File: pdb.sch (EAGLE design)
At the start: 43 parts, among them J1 XT60PWFEMALE, Q1 IRFR5305PBF, Q2 IRFR5305PBF, Q3 20MHz, U1 TSR_1-2433, U2 TXB0104, U3 ATMEGA48-20AU, U4 LTC2946CMSPBF, U5 LTC2946CMSPBF, U6 LTC2946CMSPBF, U7 AT30TS74SS8M

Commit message: fixed 3d models
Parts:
- C1, C2, C3, C4, C5, C6, C7: device resistor:C-EUC0603 -> rcl:C-EUC0603
- R1, R10, R11, R2, R6, R7, R8, R9: device resistor:R-EU_R0603 -> rcl:R-EU_R0603
- U4: SPICEPREFIX (none) -> X
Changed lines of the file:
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@@
 <part name="Q1" library="transistor-power" library_urn="urn:adsk.eagle:library:400" deviceset="IRF?5305" device="R" package3d_urn="urn:adsk.eagle:package:29503/2" value="IRFR5305PBF"/>
 <part name="D1" library="diode" library_urn="urn:adsk.eagle:library:210" deviceset="DIODE-" device="DO214BA" package3d_urn="urn:adsk.eagle:package:43453/2" value="ZD18"/>
-<part name="R2" library="resistor" library_urn="urn:adsk.eagle:library:348" deviceset="R-EU_" device="R0603" package3d_urn="urn:adsk.eagle:package:26057/1" value="10k"/>
+<part name="R2" library="rcl" library_urn="urn:adsk.eagle:library:334" deviceset="R-EU_" device="R0603" package3d_urn="urn:adsk.eagle:package:23555/2" value="10k"/>
 <part name="Q2" library="transistor-power" library_urn="urn:adsk.eagle:library:400" deviceset="IRF?5305" device="R" package3d_urn="urn:adsk.eagle:package:29503/2" value="IRFR5305PBF"/>
-<part name="R1" library="resistor" library_urn="urn:adsk.eagle:library:348" deviceset="R-EU_" device="R0603" package3d_urn="urn:adsk.eagle:package:26057/1" value="1k"/>
+<part name="R1" library="rcl" library_urn="urn:adsk.eagle:library:334" deviceset="R-EU_" device="R0603" package3d_urn="urn:adsk.eagle:package:23555/2" value="1k"/>
 <part name="GND2" library="supply1" deviceset="GND" device=""/>
 <part name="SUPPLY2" library="supply2" library_urn="urn:adsk.eagle:library:372" deviceset="V+" device=""/>
@@
 <part name="SUPPLY7" library="supply2" library_urn="urn:adsk.eagle:library:372" deviceset="+5V" device=""/>
 <part name="+3V32" library="supply1" library_urn="urn:adsk.eagle:library:371" deviceset="+3V3" device=""/>
-<part name="R6" library="resistor" library_urn="urn:adsk.eagle:library:348" deviceset="R-EU_" device="R0603" package3d_urn="urn:adsk.eagle:package:26057/1" value="1,2k"/>
-<part name="R7" library="resistor" library_urn="urn:adsk.eagle:library:348" deviceset="R-EU_" device="R0603" package3d_urn="urn:adsk.eagle:package:26057/1" value="250"/>
-<part name="R8" library="resistor" library_urn="urn:adsk.eagle:library:348" deviceset="R-EU_" device="R0603" package3d_urn="urn:adsk.eagle:package:26057/1" value="100"/>
-<part name="U4" library="niklas_lt" library_urn="urn:adsk.eagle:library:1392990" deviceset="LTC2946CMSPBF" device="" package3d_urn="urn:adsk.eagle:package:1392996/2"/>
+<part name="R6" library="rcl" library_urn="urn:adsk.eagle:library:334" deviceset="R-EU_" device="R0603" package3d_urn="urn:adsk.eagle:package:23555/2" value="1,2k"/>
+<part name="R7" library="rcl" library_urn="urn:adsk.eagle:library:334" deviceset="R-EU_" device="R0603" package3d_urn="urn:adsk.eagle:package:23555/2" value="250"/>
+<part name="R8" library="rcl" library_urn="urn:adsk.eagle:library:334" deviceset="R-EU_" device="R0603" package3d_urn="urn:adsk.eagle:package:23555/2" value="100"/>
+<part name="U4" library="niklas_lt" library_urn="urn:adsk.eagle:library:1392990" deviceset="LTC2946CMSPBF" device="" package3d_urn="urn:adsk.eagle:package:1392996/2">
+<attribute name="SPICEPREFIX" value="X"/>
+</part>
 <part name="U5" library="niklas_lt" library_urn="urn:adsk.eagle:library:1392990" deviceset="LTC2946CMSPBF" device="" package3d_urn="urn:adsk.eagle:package:1392996/2"/>
 <part name="U6" library="niklas_lt" library_urn="urn:adsk.eagle:library:1392990" deviceset="LTC2946CMSPBF" device="" package3d_urn="urn:adsk.eagle:package:1392996/2"/>
@@
 <part name="SUPPLY14" library="supply2" library_urn="urn:adsk.eagle:library:372" deviceset="+5V" device=""/>
 <part name="SUPPLY12" library="supply2" library_urn="urn:adsk.eagle:library:372" deviceset="V+" device=""/>
-<part name="C5" library="resistor" library_urn="urn:adsk.eagle:library:348" deviceset="C-EU" device="C0603" package3d_urn="urn:adsk.eagle:package:26138/1" value="0,1µF"/>
-<part name="C6" library="resistor" library_urn="urn:adsk.eagle:library:348" deviceset="C-EU" device="C0603" package3d_urn="urn:adsk.eagle:package:26138/1" value="0,1µF"/>
-<part name="C7" library="resistor" library_urn="urn:adsk.eagle:library:348" deviceset="C-EU" device="C0603" package3d_urn="urn:adsk.eagle:package:26138/1" value="0,1µF"/>
+<part name="C5" library="rcl" library_urn="urn:adsk.eagle:library:334" deviceset="C-EU" device="C0603" package3d_urn="urn:adsk.eagle:package:23616/2" value="0,1µF"/>
+<part name="C6" library="rcl" library_urn="urn:adsk.eagle:library:334" deviceset="C-EU" device="C0603" package3d_urn="urn:adsk.eagle:package:23616/2" value="0,1µF"/>
+<part name="C7" library="rcl" library_urn="urn:adsk.eagle:library:334" deviceset="C-EU" device="C0603" package3d_urn="urn:adsk.eagle:package:23616/2" value="0,1µF"/>
 <part name="GND13" library="supply1" library_urn="urn:adsk.eagle:library:371" deviceset="GND" device=""/>
 <part name="GND12" library="supply1" library_urn="urn:adsk.eagle:library:371" deviceset="GND" device=""/>
@@
 <part name="Q3" library="crystal" library_urn="urn:adsk.eagle:library:204" deviceset="CRYSTAL" device="HC49UP" package3d_urn="urn:adsk.eagle:package:12078/1" value="20MHz"/>
 <part name="GND10" library="supply1" library_urn="urn:adsk.eagle:library:371" deviceset="GND" device=""/>
-<part name="C3" library="resistor" library_urn="urn:adsk.eagle:library:348" deviceset="C-EU" device="C0603" package3d_urn="urn:adsk.eagle:package:26138/1" value="22pF"/>
-<part name="C4" library="resistor" library_urn="urn:adsk.eagle:library:348" deviceset="C-EU" device="C0603" package3d_urn="urn:adsk.eagle:package:26138/1" value="22pF"/>
+<part name="C3" library="rcl" library_urn="urn:adsk.eagle:library:334" deviceset="C-EU" device="C0603" package3d_urn="urn:adsk.eagle:package:23616/2" value="22pF"/>
+<part name="C4" library="rcl" library_urn="urn:adsk.eagle:library:334" deviceset="C-EU" device="C0603" package3d_urn="urn:adsk.eagle:package:23616/2" value="22pF"/>
 <part name="SUPPLY9" library="supply2" deviceset="+5V" device=""/>
 <part name="SUPPLY8" library="supply2" deviceset="+5V" device=""/>
@@
 <part name="GND16" library="supply1" library_urn="urn:adsk.eagle:library:371" deviceset="GND" device=""/>
 <part name="SUPPLY15" library="supply2" library_urn="urn:adsk.eagle:library:372" deviceset="+5V" device=""/>
-<part name="R11" library="resistor" library_urn="urn:adsk.eagle:library:348" deviceset="R-EU_" device="R0603" package3d_urn="urn:adsk.eagle:package:26057/1" value="4,7k"/>
-<part name="R10" library="resistor" library_urn="urn:adsk.eagle:library:348" deviceset="R-EU_" device="R0603" package3d_urn="urn:adsk.eagle:package:26057/1" value="4,7k"/>
-<part name="R9" library="resistor" library_urn="urn:adsk.eagle:library:348" deviceset="R-EU_" device="R0603" package3d_urn="urn:adsk.eagle:package:26057/1" value="4,7k"/>
+<part name="R11" library="rcl" library_urn="urn:adsk.eagle:library:334" deviceset="R-EU_" device="R0603" package3d_urn="urn:adsk.eagle:package:23555/2" value="4,7k"/>
+<part name="R10" library="rcl" library_urn="urn:adsk.eagle:library:334" deviceset="R-EU_" device="R0603" package3d_urn="urn:adsk.eagle:package:23555/2" value="4,7k"/>
+<part name="R9" library="rcl" library_urn="urn:adsk.eagle:library:334" deviceset="R-EU_" device="R0603" package3d_urn="urn:adsk.eagle:package:23555/2" value="4,7k"/>
 <part name="GND9" library="supply1" library_urn="urn:adsk.eagle:library:371" deviceset="GND" device=""/>
 <part name="SUPPLY10" library="supply2" deviceset="+5V" device=""/>
@@
 <part name="ISP" library="pinhead" library_urn="urn:adsk.eagle:library:325" deviceset="PINHD-2X3" device="/90" package3d_urn="urn:adsk.eagle:package:22464/2"/>
 <part name="GND7" library="supply1" library_urn="urn:adsk.eagle:library:371" deviceset="GND" device=""/>
-<part name="C1" library="resistor" library_urn="urn:adsk.eagle:library:348" deviceset="C-EU" device="C0603" package3d_urn="urn:adsk.eagle:package:26138/1" value="100nF"/>
-<part name="C2" library="resistor" library_urn="urn:adsk.eagle:library:348" deviceset="C-EU" device="C0603" package3d_urn="urn:adsk.eagle:package:26138/1" value="100nF"/>
+<part name="C1" library="rcl" library_urn="urn:adsk.eagle:library:334" deviceset="C-EU" device="C0603" package3d_urn="urn:adsk.eagle:package:23616/2" value="100nF"/>
+<part name="C2" library="rcl" library_urn="urn:adsk.eagle:library:334" deviceset="C-EU" device="C0603" package3d_urn="urn:adsk.eagle:package:23616/2" value="100nF"/>
 <part name="JP1" library="pinhead" library_urn="urn:adsk.eagle:library:325" deviceset="PINHD-1X2" device="" package3d_urn="urn:adsk.eagle:package:22435/2"/>
 <part name="JP3" library="pinhead" library_urn="urn:adsk.eagle:library:325" deviceset="PINHD-1X2" device="" package3d_urn="urn:adsk.eagle:package:22435/2"/>
@@
 packages will not be understood (or retained) with this version.
 </note>
+<note version="8.4" severity="warning">
+Since Version 8.4, EAGLE supports properties for SPICE simulation.
+Probes in schematics and SPICE mapping objects found in parts and library devices
+will not be understood with this version. Update EAGLE to the latest version
+for full support of SPICE simulation.
+</note>
 </compatibility>

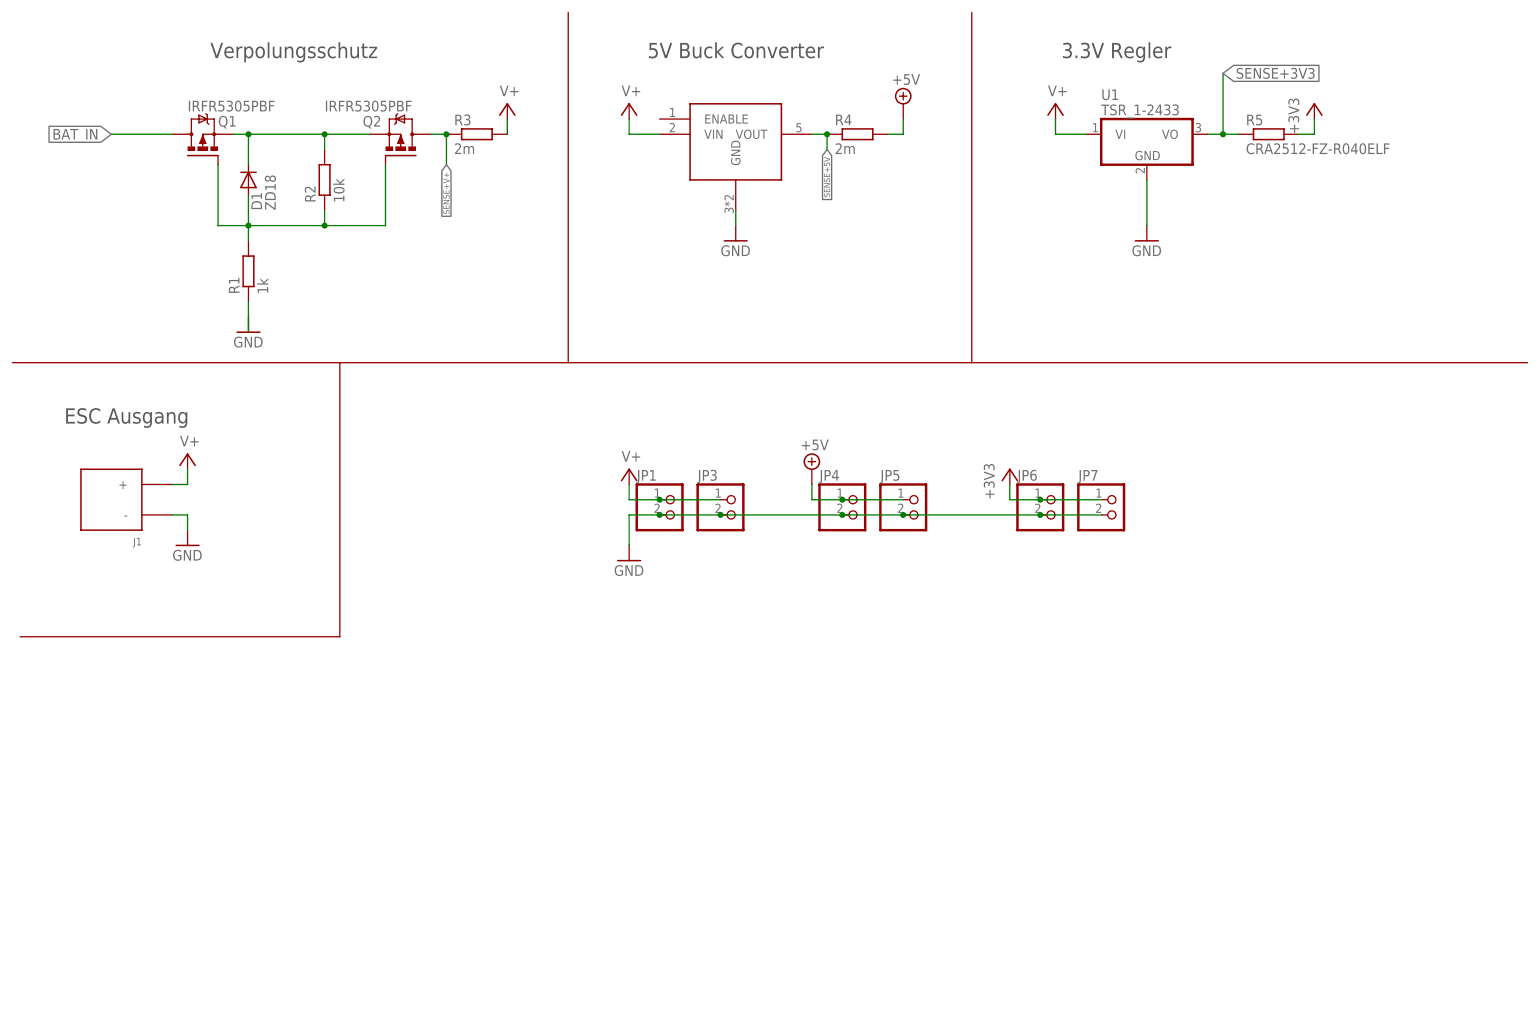
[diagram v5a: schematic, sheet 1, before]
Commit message: added reset, closed #11
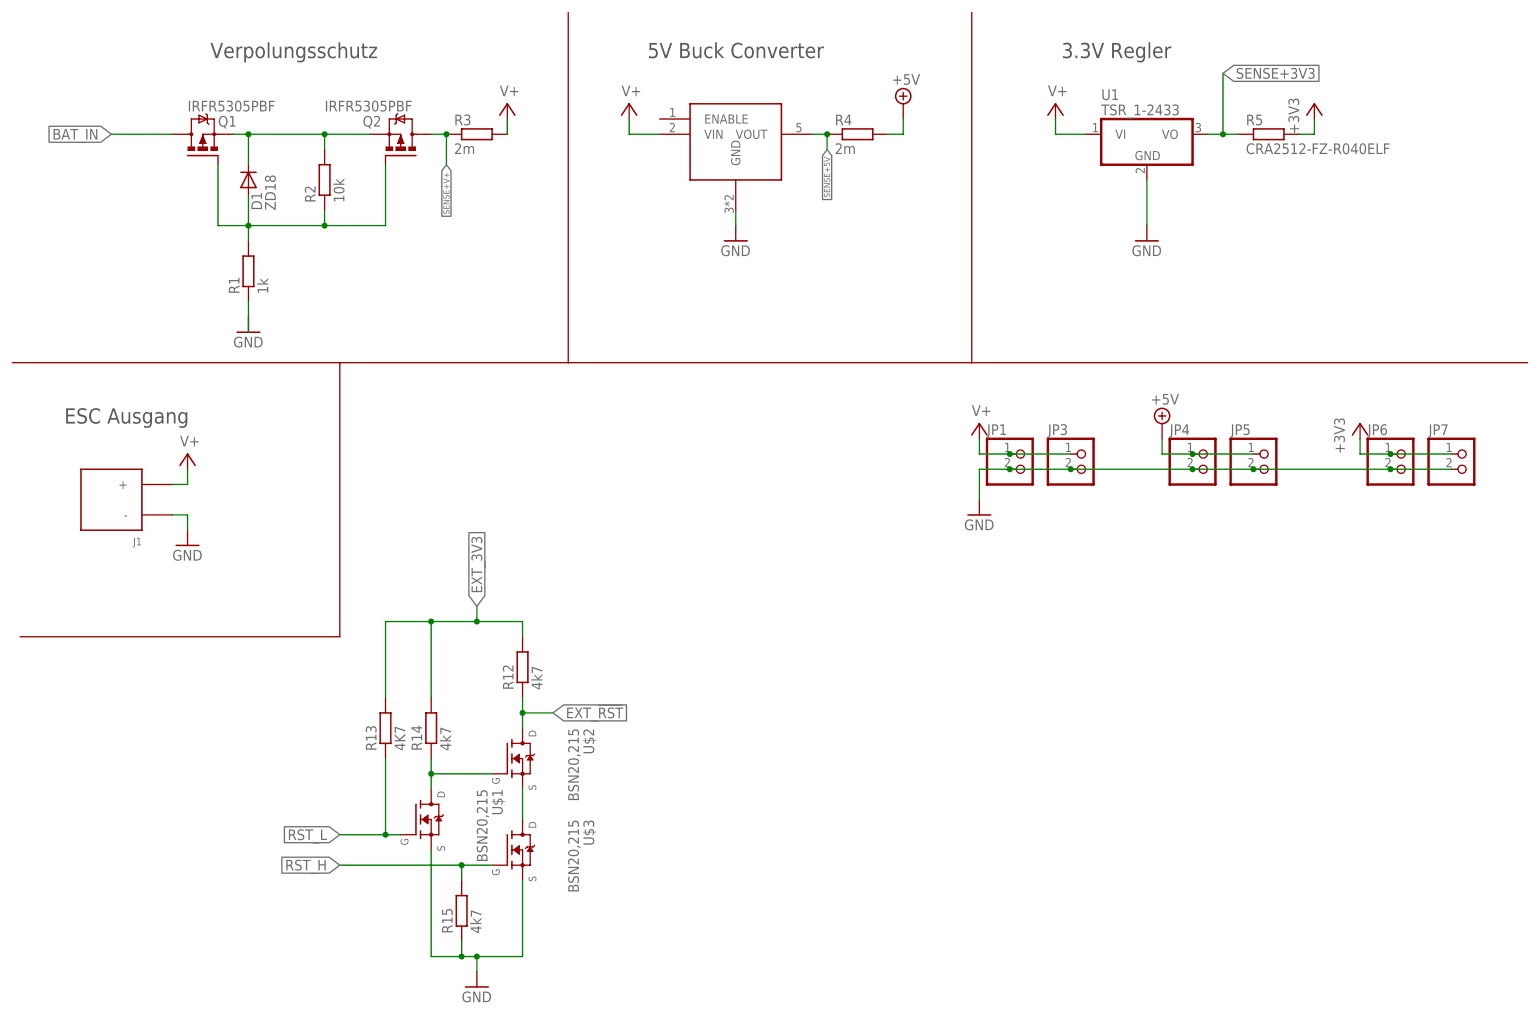
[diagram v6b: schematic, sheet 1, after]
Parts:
- added R12, R14, R15: 4k7, rcl:R-EU_R0603
- added R13: 4K7, rcl:R-EU_R0603
- added U$1, U$2, U$3: BSN20,215, jonas_mosfet:BSN20,215
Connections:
- new net N$11: U$2.S, U$3.D
- new net N$9: R14.1, U$1.D, U$2.G
- new net RST_H: R15.2, U$3.G, U3A.(PCINT22/OC0A/AIN0)_PD6
- new net RST_L: R13.1, U$1.G, U3A.(PCINT23/AIN1)_PD7
- net EXT_!RST: now also R12.1, U$2.D
- net EXT_3V3: now also R12.2, R13.2, R14.2
- net GND: now also R15.1, U$1.S, U$3.S
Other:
- moved on the sheet: JP1, JP3, JP4, JP5, JP6, JP7

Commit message: silkscreen
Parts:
- removed U$3: BSN20,215, jonas_mosfet:BSN20,215
- added XTAL1: 20MHz, crystal:CRYSTALHC49UP
- Q3: value 20MHz -> BSN20,215; device crystal:CRYSTALHC49UP -> jonas_mosfet:BSN20,215
- renumbered U$1 to Q4, U$2 to Q5
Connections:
- net GND: now also Q3.S; no longer U$3.S
- net N$11: now also Q3.D; no longer U$3.D
- net N$27: now also XTAL1.2; no longer Q3.2
- net N$28: now also XTAL1.1; no longer Q3.1
- net RST_H: now also Q3.G; no longer U$3.G
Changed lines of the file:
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@@
 <part name="FRAME1" library="frames" library_urn="urn:adsk.eagle:library:229" deviceset="A4L-LOC" device=""/>
 <part name="U2" library="SparkFun-IC-Comms" library_urn="urn:adsk.eagle:library:521" deviceset="TXB0104PWR" device="" package3d_urn="urn:adsk.eagle:package:38732/1" value="TXB0104"/>
-<part name="Q3" library="crystal" library_urn="urn:adsk.eagle:library:204" deviceset="CRYSTAL" device="HC49UP" package3d_urn="urn:adsk.eagle:package:12078/1" value="20MHz"/>
+<part name="XTAL1" library="crystal" library_urn="urn:adsk.eagle:library:204" deviceset="CRYSTAL" device="HC49UP" package3d_urn="urn:adsk.eagle:package:12078/1" value="20MHz"/>
 <part name="GND10" library="supply1" library_urn="urn:adsk.eagle:library:371" deviceset="GND" device=""/>
 <part name="C3" library="rcl" library_urn="urn:adsk.eagle:library:334" deviceset="C-EU" device="C0603" package3d_urn="urn:adsk.eagle:package:23616/2" value="22pF"/>
@@
 <part name="R13" library="rcl" library_urn="urn:adsk.eagle:library:334" deviceset="R-EU_" device="R0603" package3d_urn="urn:adsk.eagle:package:23555/2" value="4K7"/>
 <part name="R15" library="rcl" library_urn="urn:adsk.eagle:library:334" deviceset="R-EU_" device="R0603" package3d_urn="urn:adsk.eagle:package:23555/2" value="4k7"/>
-<part name="U$1" library="jonas_mosfet" library_urn="urn:adsk.eagle:library:2195717" deviceset="BSN20,215" device="" package3d_urn="urn:adsk.eagle:package:2195720/2"/>
-<part name="U$2" library="jonas_mosfet" library_urn="urn:adsk.eagle:library:2195717" deviceset="BSN20,215" device="" package3d_urn="urn:adsk.eagle:package:2195720/2"/>
-<part name="U$3" library="jonas_mosfet" library_urn="urn:adsk.eagle:library:2195717" deviceset="BSN20,215" device="" package3d_urn="urn:adsk.eagle:package:2195720/2"/>
+<part name="Q4" library="jonas_mosfet" library_urn="urn:adsk.eagle:library:2195717" deviceset="BSN20,215" device="" package3d_urn="urn:adsk.eagle:package:2195720/3"/>
+<part name="Q5" library="jonas_mosfet" library_urn="urn:adsk.eagle:library:2195717" deviceset="BSN20,215" device="" package3d_urn="urn:adsk.eagle:package:2195720/3"/>
+<part name="Q3" library="jonas_mosfet" library_urn="urn:adsk.eagle:library:2195717" deviceset="BSN20,215" device="" package3d_urn="urn:adsk.eagle:package:2195720/3"/>
 <part name="GND21" library="supply1" deviceset="GND" device=""/>
 </parts>
@@
 <instance part="R13" gate="G$1" x="-60.96" y="5.08" rot="R90"/>
 <instance part="R15" gate="G$1" x="-48.26" y="-25.4" rot="R90"/>
-<instance part="U$1" gate="G$1" x="-50.8" y="-10.16" rot="R270"/>
-<instance part="U$2" gate="G$1" x="-35.56" y="0" rot="R270"/>
-<instance part="U$3" gate="G$1" x="-35.56" y="-15.24" rot="R270"/>
+<instance part="Q4" gate="G$1" x="-50.8" y="-10.16" rot="R270"/>
+<instance part="Q5" gate="G$1" x="-35.56" y="0" rot="R270"/>
+<instance part="Q3" gate="G$1" x="-35.56" y="-15.24" rot="R270"/>
 <instance part="GND21" gate="1" x="-45.72" y="-38.1"/>
 </instances>
@@
 <wire x1="-48.26" y1="-30.48" x2="-48.26" y2="-33.02" width="0.1524" layer="91"/>
 <junction x="-48.26" y="-33.02"/>
-<pinref part="U$3" gate="G$1" pin="S"/>
-<pinref part="U$1" gate="G$1" pin="S"/>
+<pinref part="Q3" gate="G$1" pin="S"/>
+<pinref part="Q4" gate="G$1" pin="S"/>
 <wire x1="-53.34" y1="-15.24" x2="-53.34" y2="-33.02" width="0.1524" layer="91"/>
 <wire x1="-45.72" y1="-33.02" x2="-45.72" y2="-35.56" width="0.1524" layer="91"/>
@@
 <wire x1="-60.96" y1="0" x2="-60.96" y2="-12.7" width="0.1524" layer="91"/>
 <junction x="-60.96" y="-12.7"/>
-<pinref part="U$1" gate="G$1" pin="G"/>
+<pinref part="Q4" gate="G$1" pin="G"/>
 <label x="-68.58" y="-12.7" size="1.778" layer="95" rot="R180" xref="yes"/>
 </segment>
@@
 <wire x1="-38.1" y1="10.16" x2="-38.1" y2="7.62" width="0.1524" layer="91"/>
 <wire x1="-38.1" y1="7.62" x2="-38.1" y2="5.08" width="0.1524" layer="91"/>
-<pinref part="U$2" gate="G$1" pin="D"/>
+<pinref part="Q5" gate="G$1" pin="D"/>
 <wire x1="-38.1" y1="7.62" x2="-33.02" y2="7.62" width="0.1524" layer="91"/>
 <junction x="-38.1" y="7.62"/>
@@
 <wire x1="-53.34" y1="-2.54" x2="-43.18" y2="-2.54" width="0.1524" layer="91"/>
 <junction x="-53.34" y="-2.54"/>
-<pinref part="U$1" gate="G$1" pin="D"/>
-<pinref part="U$2" gate="G$1" pin="G"/>
+<pinref part="Q4" gate="G$1" pin="D"/>
+<pinref part="Q5" gate="G$1" pin="G"/>
 </segment>
 </net>
@@
 <pinref part="R15" gate="G$1" pin="2"/>
 <wire x1="-48.26" y1="-20.32" x2="-48.26" y2="-17.78" width="0.1524" layer="91"/>
-<pinref part="U$3" gate="G$1" pin="G"/>
+<pinref part="Q3" gate="G$1" pin="G"/>
 <wire x1="-43.18" y1="-17.78" x2="-48.26" y2="-17.78" width="0.1524" layer="91"/>
 <wire x1="-48.26" y1="-17.78" x2="-68.58" y2="-17.78" width="0.1524" layer="91"/>
@@
 <net name="N$11" class="0">
 <segment>
-<pinref part="U$2" gate="G$1" pin="S"/>
-<pinref part="U$3" gate="G$1" pin="D"/>
+<pinref part="Q5" gate="G$1" pin="S"/>
+<pinref part="Q3" gate="G$1" pin="D"/>
 <wire x1="-38.1" y1="-5.08" x2="-38.1" y2="-10.16" width="0.1524" layer="91"/>
 </segment>
@@
 <instance part="FRAME2" gate="G$1" x="0" y="0"/>
 <instance part="U2" gate="G$1" x="43.18" y="66.04"/>
-<instance part="Q3" gate="G$1" x="215.9" y="144.78" rot="R90"/>
+<instance part="XTAL1" gate="G$1" x="215.9" y="144.78" rot="R90"/>
 <instance part="GND10" gate="1" x="226.06" y="137.16"/>
 <instance part="C3" gate="G$1" x="220.98" y="147.32" rot="R90"/>
@@
 <segment>
 <pinref part="U3" gate="A" pin="(PCINT6/XTAL1/TOSC1)_PB6"/>
-<pinref part="Q3" gate="G$1" pin="2"/>
+<pinref part="XTAL1" gate="G$1" pin="2"/>
 <wire x1="200.66" y1="147.32" x2="215.9" y2="147.32" width="0.1524" layer="91"/>
 <wire x1="215.9" y1="147.32" x2="218.44" y2="147.32" width="0.1524" layer="91"/>
@@
 <wire x1="200.66" y1="144.78" x2="210.82" y2="144.78" width="0.1524" layer="91"/>
 <wire x1="210.82" y1="144.78" x2="210.82" y2="142.24" width="0.1524" layer="91"/>
-<pinref part="Q3" gate="G$1" pin="1"/>
+<pinref part="XTAL1" gate="G$1" pin="1"/>
 <wire x1="210.82" y1="142.24" x2="215.9" y2="142.24" width="0.1524" layer="91"/>
 <wire x1="215.9" y1="142.24" x2="218.44" y2="142.24" width="0.1524" layer="91"/>
